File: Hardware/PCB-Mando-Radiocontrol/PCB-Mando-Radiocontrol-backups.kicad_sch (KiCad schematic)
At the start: 25 parts, among them J1 USB 2.0 a UART TTL 6 pines CP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, J2 ALIMENTACION, SW1 SW_SPDT, SW2 SW_SPDT, SW3 SW_SPDT, U1 ATMEGA328P, U2 Nrf24l01, U3 AMS1117-3.3, U4 AMS1117-5.0, U5 COM-09032, U6 COM-09032, Y1 16MHZ

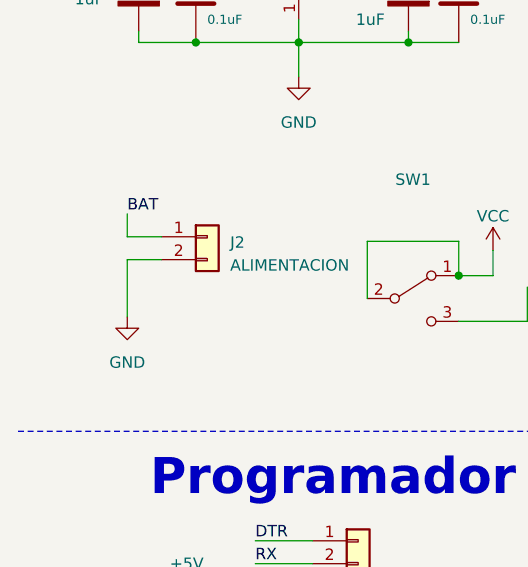
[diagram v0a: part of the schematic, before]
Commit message: PCB a medida con componentes a ordenar
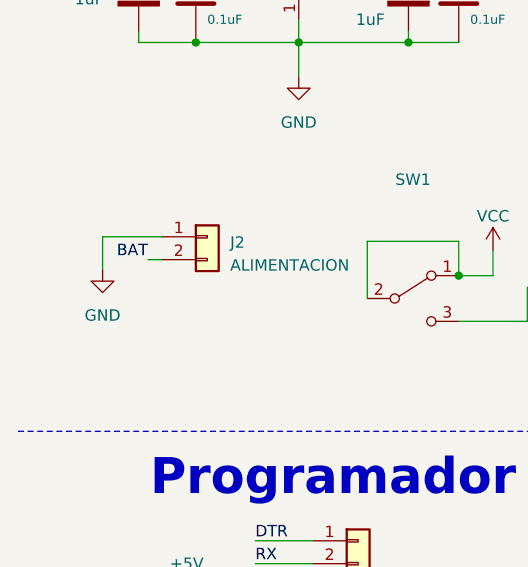
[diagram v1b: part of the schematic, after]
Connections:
- net BAT: now also J2.2 (Pin_2); no longer J2.1 (Pin_1)
- net GND: now also J2.1 (Pin_1); no longer J2.2 (Pin_2)
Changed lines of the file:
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@@
-    (stroke (width 0) (type default))
-  )
-  (wire (pts (xy 24.13 114.3) (xy 24.13 107.95))
     (stroke (width 0) (type default))
   )
@@
     (stroke (width 0) (type default))
   )
+  (wire (pts (xy 21.3868 105.41) (xy 27.94 105.41))
+    (stroke (width 0) (type default))
+  )
   (wire (pts (xy 237.49 40.64) (xy 237.49 39.37))
     (stroke (width 0) (type default))
@@
     (stroke (width 0) (type default))
   )
-  (wire (pts (xy 24.13 107.95) (xy 27.94 107.95))
-    (stroke (width 0) (type default))
-  )
   (wire (pts (xy 90.17 95.25) (xy 90.17 102.108))
     (stroke (width 0) (type default))
   )
   (wire (pts (xy 242.57 54.61) (xy 242.57 58.42))
-    (stroke (width 0) (type default))
-  )
-  (wire (pts (xy 27.94 105.41) (xy 24.13 105.41))
     (stroke (width 0) (type default))
   )
@@
     (stroke (width 0) (type default))
   )
+  (wire (pts (xy 26.416 107.95) (xy 27.94 107.95))
+    (stroke (width 0) (type default))
+  )
   (wire (pts (xy 233.68 43.18) (xy 233.68 46.99))
     (stroke (width 0) (type default))
@@
   )
   (wire (pts (xy 43.18 83.82) (xy 43.18 81.28))
-    (stroke (width 0) (type default))
-  )
-  (wire (pts (xy 24.13 102.87) (xy 24.13 105.41))
     (stroke (width 0) (type default))
   )
@@
   )
   (wire (pts (xy 55.372 73.66) (xy 60.96 73.66))
+    (stroke (width 0) (type default))
+  )
+  (wire (pts (xy 21.3868 109.0676) (xy 21.3868 105.41))
     (stroke (width 0) (type default))
   )
@@
     (effects (font (size 3 3) (thickness 0.6) bold) (justify left bottom))
   )
+  (label "BAT" (at 26.416 107.95 180) (fields_autoplaced)
+    (effects (font (size 1.27 1.27)) (justify right bottom))
+  )
   (label "SCK" (at 212.09 107.95 0) (fields_autoplaced)
     (effects (font (size 1.27 1.27)) (justify left bottom))
@@
   )
   (label "MISO" (at 149.86 93.98 0) (fields_autoplaced)
-    (effects (font (size 1.27 1.27)) (justify left bottom))
-  )
-  (label "BAT" (at 24.13 102.87 0) (fields_autoplaced)
     (effects (font (size 1.27 1.27)) (justify left bottom))
   )
@@
     )
   )
+  (symbol (lib_id "power:GND") (at 21.3868 109.0676 0) (unit 1)
+    (in_bom yes) (on_board yes) (dnp no) (fields_autoplaced)
+    (property "Reference" "#PWR03" (at 21.3868 115.4176 0)
+      (effects (font (size 1.27 1.27)) hide)
+    )
+    (property "Value" "GND" (at 21.3868 114.1476 0)
+      (effects (font (size 1.27 1.27)))
+    )
+    (property "Footprint" "" (at 21.3868 109.0676 0)
+      (effects (font (size 1.27 1.27)) hide)
+    )
+    (property "Datasheet" "" (at 21.3868 109.0676 0)
+      (effects (font (size 1.27 1.27)) hide)
+    )
+    (pin "1")
+    (instances
+      (project "PCB-Mando-Radiocontrol-backups"
+        (path "/a09d701e-8048-4e72-8e3a-cb0f8f921380"
+          (reference "#PWR03") (unit 1)
+        )
+      )
+    )
+  )
   (symbol (lib_id "power:GND") (at 191.77 40.64 0) (unit 1)
     (in_bom yes) (on_board yes) (dnp no) (fields_autoplaced)
@@
         )
       )
-    )
-  )
-  (symbol (lib_id "power:GND") (at 24.13 114.3 0) (unit 1)
-    (in_bom yes) (on_board yes) (dnp no) (fields_autoplaced)
-    (property "Reference" "#PWR010" (at 24.13 120.65 0)
-      (effects (font (size 1.27 1.27)) hide)
-    )
-    (property "Value" "GND" (at 24.13 119.38 0)
-      (effects (font (size 1.27 1.27)))
-    )
-    (property "Footprint" "" (at 24.13 114.3 0)
-      (effects (font (size 1.27 1.27)) hide)
-    )
-    (property "Datasheet" "" (at 24.13 114.3 0)
-      (effects (font (size 1.27 1.27)) hide)
-    )
-    (pin "1")
-    (instances
-      (project "PCB-Mando-Radiocontrol-backups"
-        (path "/a09d701e-8048-4e72-8e3a-cb0f8f921380"
-          (reference "#PWR010") (unit 1)
-        )
-      )

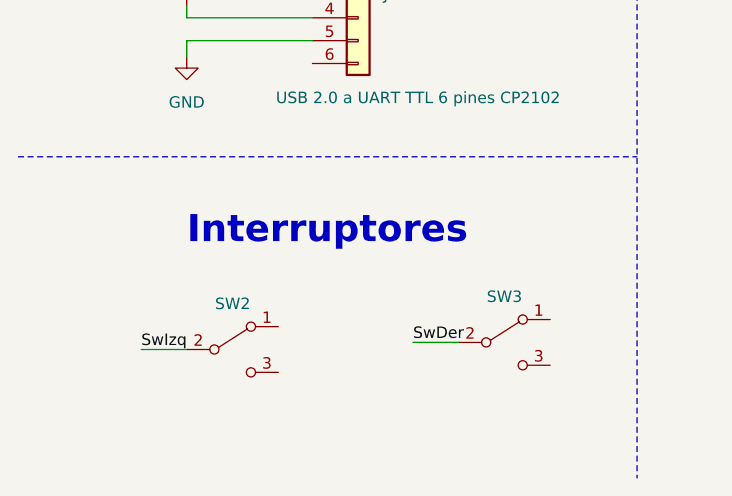
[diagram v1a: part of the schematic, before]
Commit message: Errores en el esquematico corregidos
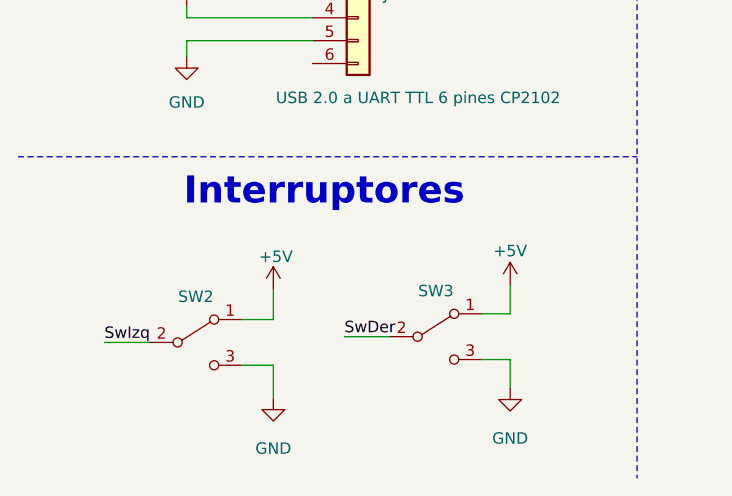
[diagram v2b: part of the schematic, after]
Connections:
- net +5V: now also SW2.1 (A), SW3.1 (A)
- net GND: now also SW2.3 (C), SW3.3 (C)
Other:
- moved on the sheet: SW2, SW3
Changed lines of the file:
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@@
     (stroke (width 0) (type default))
   )
+  (wire (pts (xy 66.675 179.705) (xy 66.675 176.53))
+    (stroke (width 0) (type default))
+  )
   (wire (pts (xy 30.734 151.13) (xy 30.734 149.352))
     (stroke (width 0) (type default))
@@
     (stroke (width 0) (type default))
   )
+  (wire (pts (xy 66.675 184.785) (xy 66.675 187.96))
+    (stroke (width 0) (type default))
+  )
   (wire (pts (xy 119.38 57.15) (xy 119.38 66.04))
     (stroke (width 0) (type default))
@@
     (stroke (width 0) (type default))
   )
-  (wire (pts (xy 25.6794 183.6674) (xy 30.7594 183.6674))
+  (wire (pts (xy 21.59 182.88) (xy 26.67 182.88))
     (stroke (width 0) (type default))
   )
@@
     (stroke (width 0) (type default))
   )
-  (wire (pts (xy 55.88 182.88) (xy 60.96 182.88))
+  (wire (pts (xy 48.26 182.245) (xy 53.34 182.245))
     (stroke (width 0) (type default))
   )
@@
     (stroke (width 0) (type default))
   )
+  (wire (pts (xy 63.5 184.785) (xy 66.675 184.785))
+    (stroke (width 0) (type default))
+  )
   (wire (pts (xy 107.95 69.85) (xy 90.17 69.85))
     (stroke (width 0) (type default))
@@
     (stroke (width 0) (type default))
   )
+  (wire (pts (xy 66.675 179.705) (xy 63.5 179.705))
+    (stroke (width 0) (type default))
+  )
+  (wire (pts (xy 40.3606 180.34) (xy 40.3606 177.0126))
+    (stroke (width 0) (type default))
+  )
   (wire (pts (xy 118.11 66.04) (xy 119.38 66.04))
     (stroke (width 0) (type default))
@@
     (stroke (width 0) (type default))
   )
+  (wire (pts (xy 40.3606 189.0776) (xy 40.3606 185.42))
+    (stroke (width 0) (type default))
+  )
   (wire (pts (xy 212.09 110.49) (xy 218.44 110.49))
     (stroke (width 0) (type default))
   )
+  (wire (pts (xy 40.3606 185.42) (xy 36.83 185.42))
+    (stroke (width 0) (type default))
+  )
   (wire (pts (xy 25.4 82.55) (xy 25.4 83.82))
     (stroke (width 0) (type default))
@@
     (stroke (width 0) (type default))
   )
+  (wire (pts (xy 36.83 180.34) (xy 40.3606 180.34))
+    (stroke (width 0) (type default))
+  )
   (wire (pts (xy 50.8 73.66) (xy 55.372 73.66))
     (stroke (width 0) (type default))
@@
     (effects (font (size 4 4) bold) (justify left bottom))
   )
-  (text "Interruptores" (at 30.7594 172.2374 0)
+  (text "Interruptores" (at 30.4038 167.9448 0)
     (effects (font (size 3 3) bold) (justify left bottom))
   )
@@
     (effects (font (size 1.27 1.27)) (justify left bottom))
   )
-  (label "SwIzq" (at 25.6794 183.6674 0) (fields_autoplaced)
+  (label "SwIzq" (at 21.59 182.88 0) (fields_autoplaced)
     (effects (font (size 1.27 1.27)) (justify left bottom))
   )
@@
     (effects (font (size 1.27 1.27)) (justify left bottom))
   )
-  (label "SwDer" (at 55.88 182.88 0) (fields_autoplaced)
+  (label "SwDer" (at 48.26 182.245 0) (fields_autoplaced)
     (effects (font (size 1.27 1.27)) (justify left bottom))
   )
@@
     )
   )
+  (symbol (lib_id "power:GND") (at 40.3606 189.0776 0) (unit 1)
+    (in_bom yes) (on_board yes) (dnp no) (fields_autoplaced)
+    (property "Reference" "#PWR04" (at 40.3606 195.4276 0)
+      (effects (font (size 1.27 1.27)) hide)
+    )
+    (property "Value" "GND" (at 40.3606 194.6656 0)
+      (effects (font (size 1.27 1.27)))
+    )
+    (property "Footprint" "" (at 40.3606 189.0776 0)
+      (effects (font (size 1.27 1.27)) hide)
+    )
+    (property "Datasheet" "" (at 40.3606 189.0776 0)
+      (effects (font (size 1.27 1.27)) hide)
+    )
+    (pin "1")
+    (instances
+      (project "PCB-Mando-Radiocontrol-backups"
+        (path "/a09d701e-8048-4e72-8e3a-cb0f8f921380"
+          (reference "#PWR04") (unit 1)
+        )
+      )
+    )
+  )
   (symbol (lib_id "power:GND") (at 229.87 124.46 0) (unit 1)
     (in_bom yes) (on_board yes) (dnp no) (fields_autoplaced)
@@
     )
   )
-  (symbol (lib_id "EESTN5:SW_SPDT") (at 66.04 182.88 0) (unit 1)
+  (symbol (lib_id "EESTN5:SW_SPDT") (at 58.42 182.245 0) (unit 1)
     (in_bom yes) (on_board yes) (dnp no)
-    (property "Reference" "SW3" (at 66.04 177.8 0)
+    (property "Reference" "SW3" (at 58.42 177.165 0)
       (effects (font (size 1.27 1.27)))
     )
-    (property "Value" "SW_SPDT" (at 66.04 187.96 0)
+    (property "Value" "SW_SPDT" (at 58.42 187.325 0)
       (effects (font (size 1.27 1.27)) hide)
     )
-    (property "Footprint" "EESTN5:Pin_Header_3" (at 66.04 182.88 0)
+    (property "Footprint" "EESTN5:Pin_Header_3" (at 58.42 182.245 0)
       (effects (font (size 1.27 1.27)) hide)
     )
-    (property "Datasheet" "" (at 66.04 182.88 0)
+    (property "Datasheet" "" (at 58.42 182.245 0)
       (effects (font (size 1.27 1.27)))
     )
@@
     )
   )
-  (symbol (lib_id "EESTN5:SW_SPDT") (at 35.8394 183.6674 0) (unit 1)
+  (symbol (lib_id "power:+5V") (at 66.675 176.53 0) (unit 1)
+    (in_bom yes) (on_board yes) (dnp no) (fields_autoplaced)
+    (property "Reference" "#PWR011" (at 66.675 180.34 0)
+      (effects (font (size 1.27 1.27)) hide)
+    )
+    (property "Value" "+5V" (at 66.675 172.72 0)
+      (effects (font (size 1.27 1.27)))
+    )
+    (property "Footprint" "" (at 66.675 176.53 0)
+      (effects (font (size 1.27 1.27)) hide)
+    )
+    (property "Datasheet" "" (at 66.675 176.53 0)
+      (effects (font (size 1.27 1.27)) hide)
+    )
+    (pin "1")
+    (instances
+      (project "PCB-Mando-Radiocontrol-backups"
+        (path "/a09d701e-8048-4e72-8e3a-cb0f8f921380"
+          (reference "#PWR011") (unit 1)
+        )
+      )
+    )
+  )
+  (symbol (lib_id "EESTN5:SW_SPDT") (at 31.75 182.88 0) (unit 1)
     (in_bom yes) (on_board yes) (dnp no)
-    (property "Reference" "SW2" (at 35.8394 178.5874 0)
+    (property "Reference" "SW2" (at 31.75 177.8 0)
       (effects (font (size 1.27 1.27)))
     )
-    (property "Value" "SW_SPDT" (at 35.8394 188.7474 0)
+    (property "Value" "SW_SPDT" (at 31.75 187.96 0)
       (effects (font (size 1.27 1.27)) hide)
     )
-    (property "Footprint" "EESTN5:Pin_Header_3" (at 35.8394 183.6674 0)
+    (property "Footprint" "EESTN5:Pin_Header_3" (at 31.75 182.88 0)
       (effects (font (size 1.27 1.27)) hide)
     )
-    (property "Datasheet" "" (at 35.8394 183.6674 0)
+    (property "Datasheet" "" (at 31.75 182.88 0)
       (effects (font (size 1.27 1.27)))
     )
@@
     )
   )
+  (symbol (lib_id "power:+5V") (at 40.3606 177.0126 0) (unit 1)
+    (in_bom yes) (on_board yes) (dnp no)
+    (property "Reference" "#PWR09" (at 40.3606 180.8226 0)
+      (effects (font (size 1.27 1.27)) hide)
+    )
+    (property "Value" "+5V" (at 40.64 173.355 0)
+      (effects (font (size 1.27 1.27)))
+    )
+    (property "Footprint" "" (at 40.3606 177.0126 0)
+      (effects (font (size 1.27 1.27)) hide)
+    )
+    (property "Datasheet" "" (at 40.3606 177.0126 0)
+      (effects (font (size 1.27 1.27)) hide)
+    )
+    (pin "1")
+    (instances
+      (project "PCB-Mando-Radiocontrol-backups"
+        (path "/a09d701e-8048-4e72-8e3a-cb0f8f921380"
+          (reference "#PWR09") (unit 1)
+        )
+      )
+    )
+  )
   (symbol (lib_id "Device:C_Polarized") (at 25.4 78.74 0) (unit 1)
     (in_bom yes) (on_board yes) (dnp no)
@@
         )
       )
+    )
+  )
+  (symbol (lib_id "power:GND") (at 66.675 187.96 0) (unit 1)
+    (in_bom yes) (on_board yes) (dnp no) (fields_autoplaced)
+    (property "Reference" "#PWR010" (at 66.675 194.31 0)
+      (effects (font (size 1.27 1.27)) hide)
+    )
+    (property "Value" "GND" (at 66.675 193.548 0)
+      (effects (font (size 1.27 1.27)))
+    )
+    (property "Footprint" "" (at 66.675 187.96 0)
+      (effects (font (size 1.27 1.27)) hide)
+    )
+    (property "Datasheet" "" (at 66.675 187.96 0)
+      (effects (font (size 1.27 1.27)) hide)
+    )
+    (pin "1")
+    (instances
+      (project "PCB-Mando-Radiocontrol-backups"
+        (path "/a09d701e-8048-4e72-8e3a-cb0f8f921380"
+          (reference "#PWR010") (unit 1)
+        )
+      )

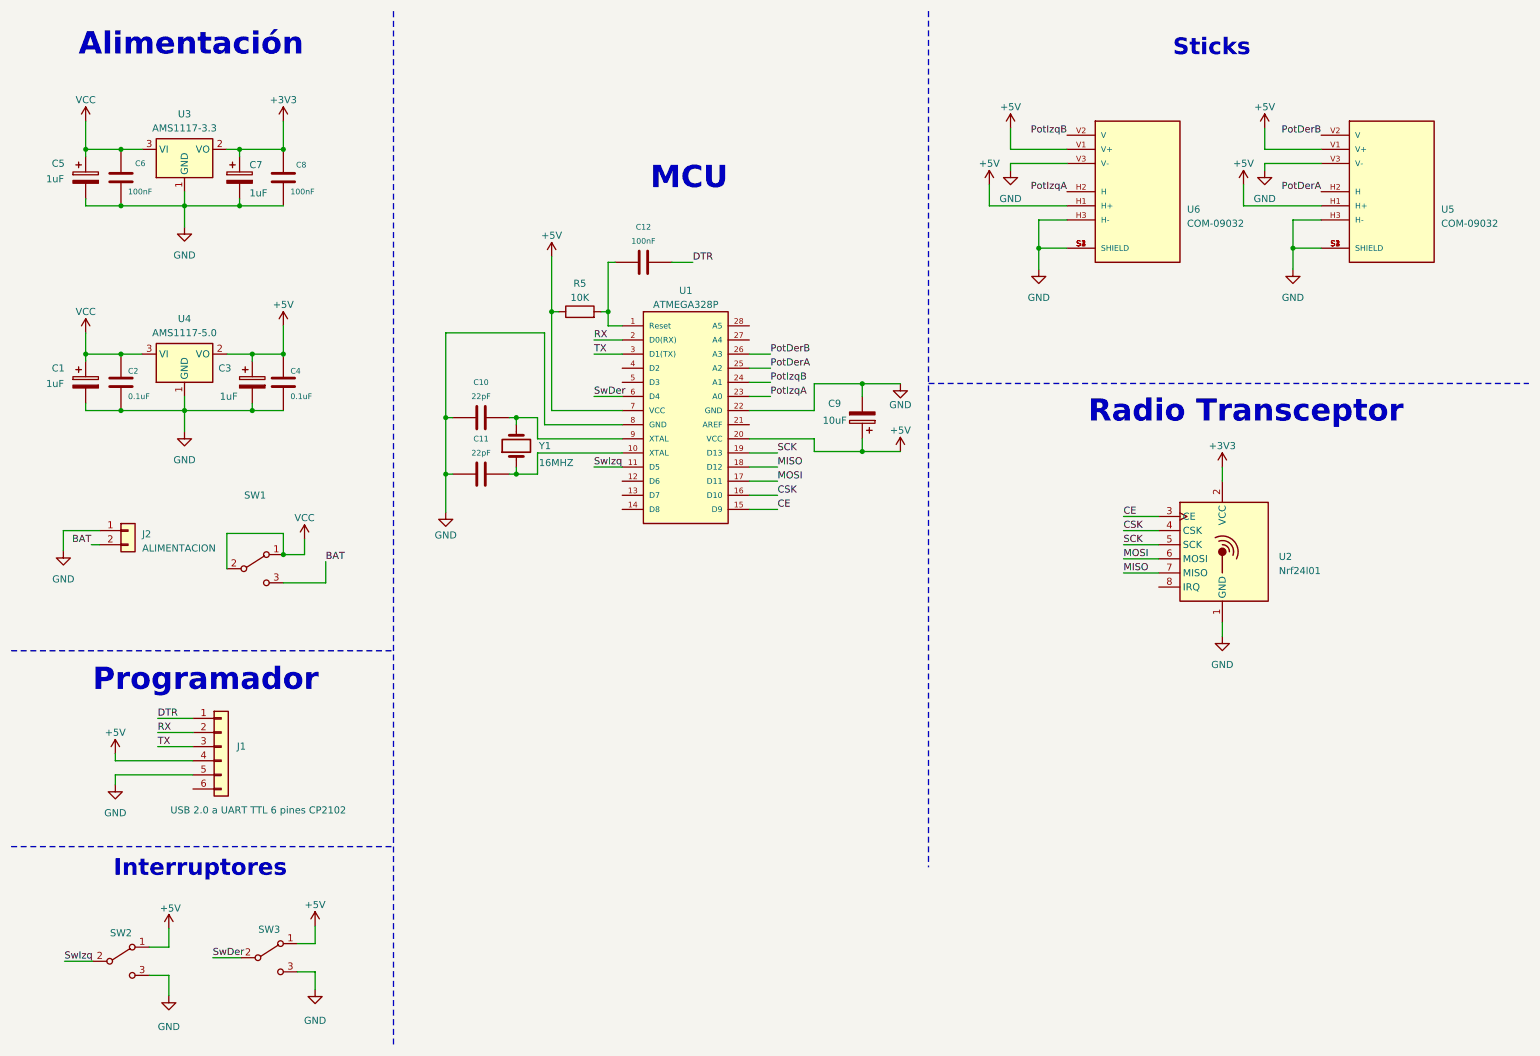
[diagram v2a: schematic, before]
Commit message: SCH corregido, PCB en proceso a falta de NRF
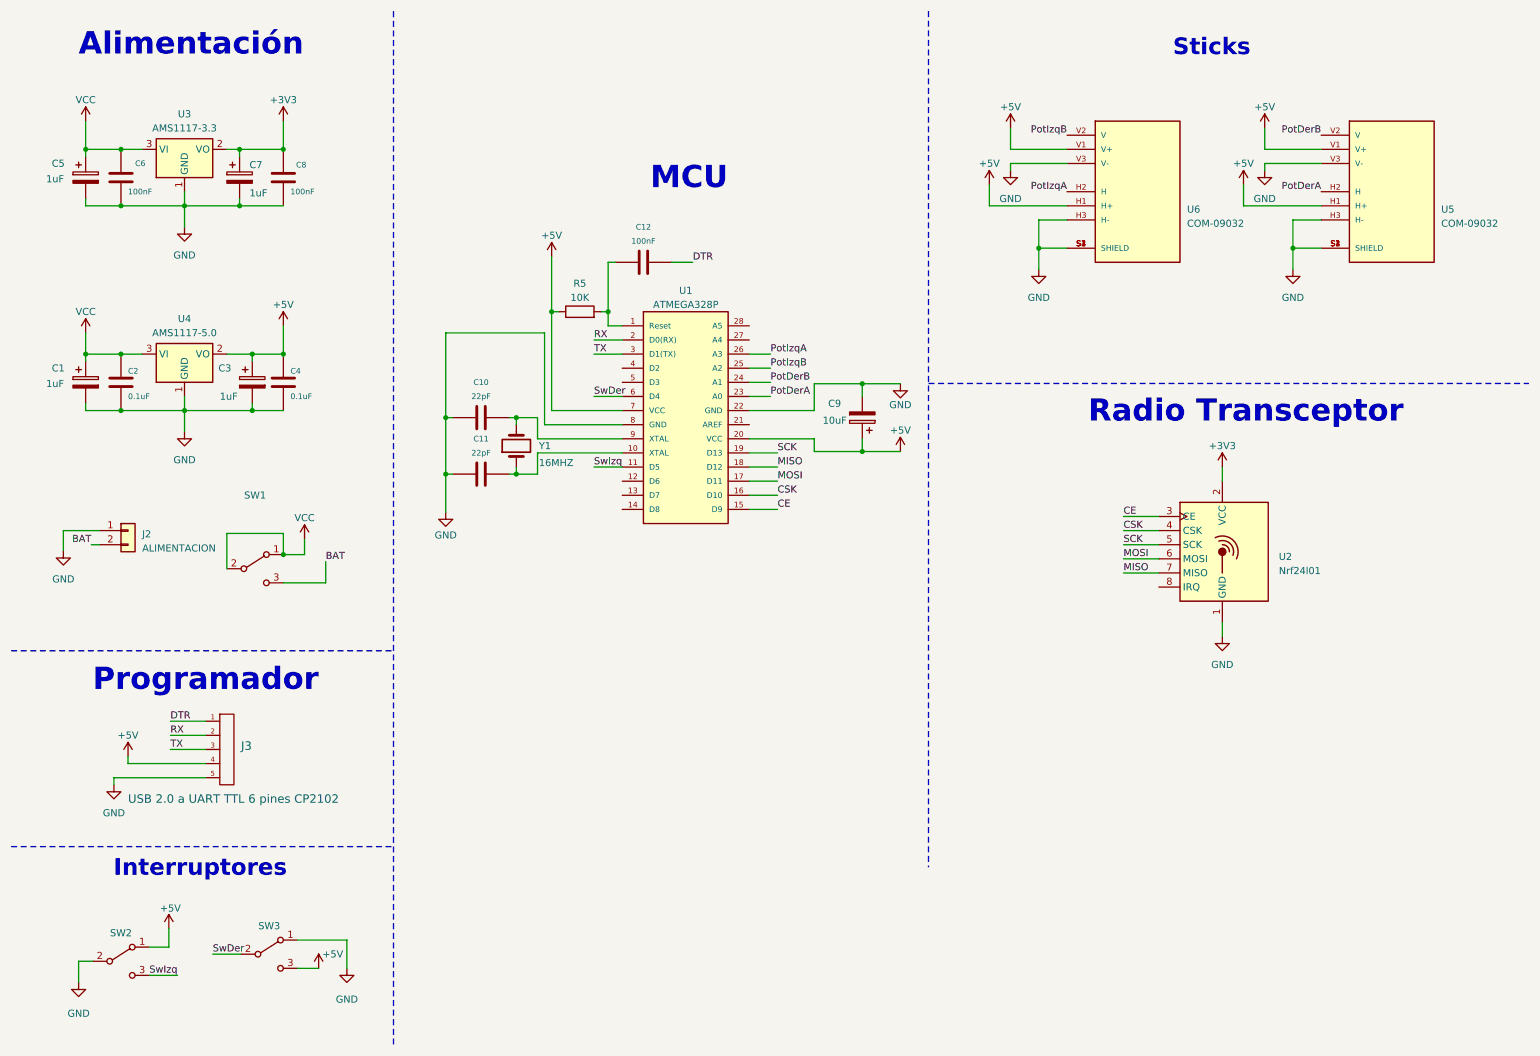
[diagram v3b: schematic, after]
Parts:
- removed J1: USB 2.0 a UART TTL 6 pines CP2102, EESTN5:Pin_Header_6, symbol EESTN5:Conn_01x06
- added J3: USB 2.0 a UART TTL 6 pines CP2102, EESTN5:Pin_Header_5, symbol EESTN5:HEADER_5
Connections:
- net +5V: now also SW3.3 (C), J3.4; no longer SW3.1 (A)
- net DTR: now also J3.1
- net GND: now also SW2.2 (B), SW3.1 (A), J3.5; no longer SW2.3 (C), SW3.3 (C)
- net PotDerA: now also U1.23 (A0); no longer U1.25 (A2)
- net PotDerB: now also U1.24 (A1); no longer U1.26 (A3)
- net PotIzqA: now also U1.26 (A3); no longer U1.23 (A0)
- net PotIzqB: now also U1.25 (A2); no longer U1.24 (A1)
- net RX: now also J3.2
- net SwIzq: now also SW2.3 (C); no longer SW2.2 (B)
- net TX: now also J3.3
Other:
- moved on the sheet: SW3
